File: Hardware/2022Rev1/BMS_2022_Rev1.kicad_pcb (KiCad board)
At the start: 2 copper layers, 114.3 x 124.5 mm, 106 parts, among them J1 Molex_uF_SV_03, J2 Molex_uF_SV_03, J3 Molex_uF_SV_04, J4 RJ45_LED_Shielded, J5 Molex_uF_SV_06, Q1 2N7000, Q3 2N7000, Q4 IRFS7530, SW2 SW_SP3T, U1 Teensy4.1_DEV-16771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

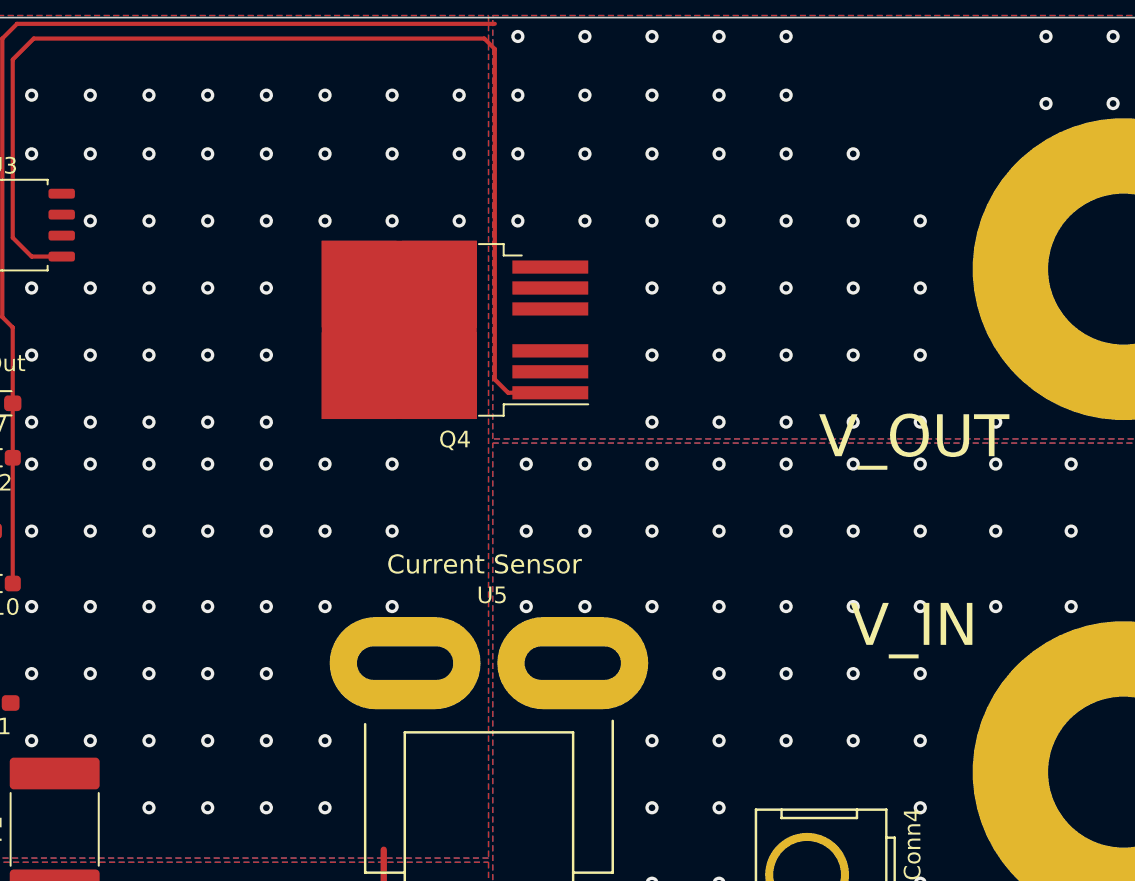
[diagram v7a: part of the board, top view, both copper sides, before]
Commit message: changed the silkscreens to face the front and checked diff pair
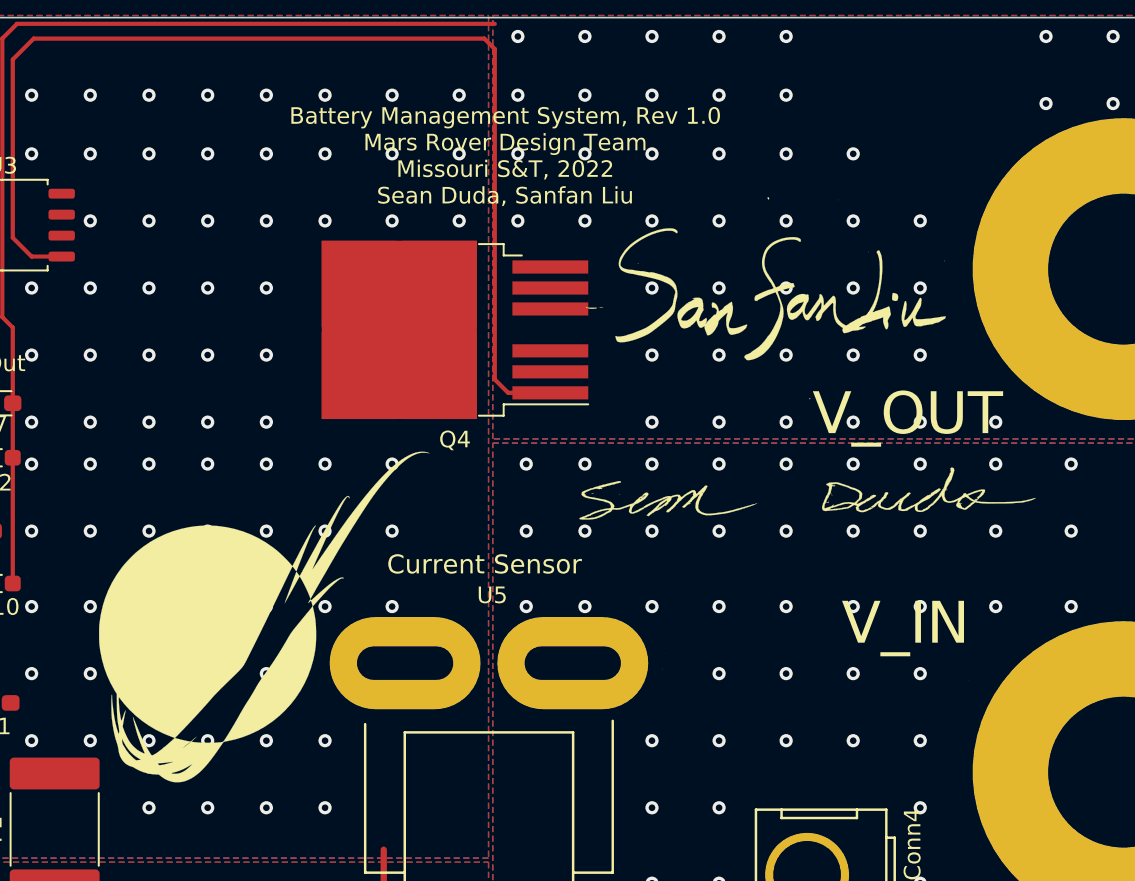
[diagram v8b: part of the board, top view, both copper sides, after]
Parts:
- removed the G*** at (-70.9, -214.1)
- added G***: LOGO, MRDT_Silkscreens:0_MRDT_Logo_20mm, F.Cu at (-71.8, -264.0)
- G*** (x2): moved to F.Cu
- moved G*** 2.79 mm to (-39.2, -271.4)
- moved G*** 0.63 mm to (-40.8, -283.6), turned to 0 degrees
